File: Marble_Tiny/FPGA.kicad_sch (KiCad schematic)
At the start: 43 parts, among them T1 BSS138LT1G, T2 BSS138LT1G, U1 XC7A35T-CSG325, U28 24AA256UID-I_ST

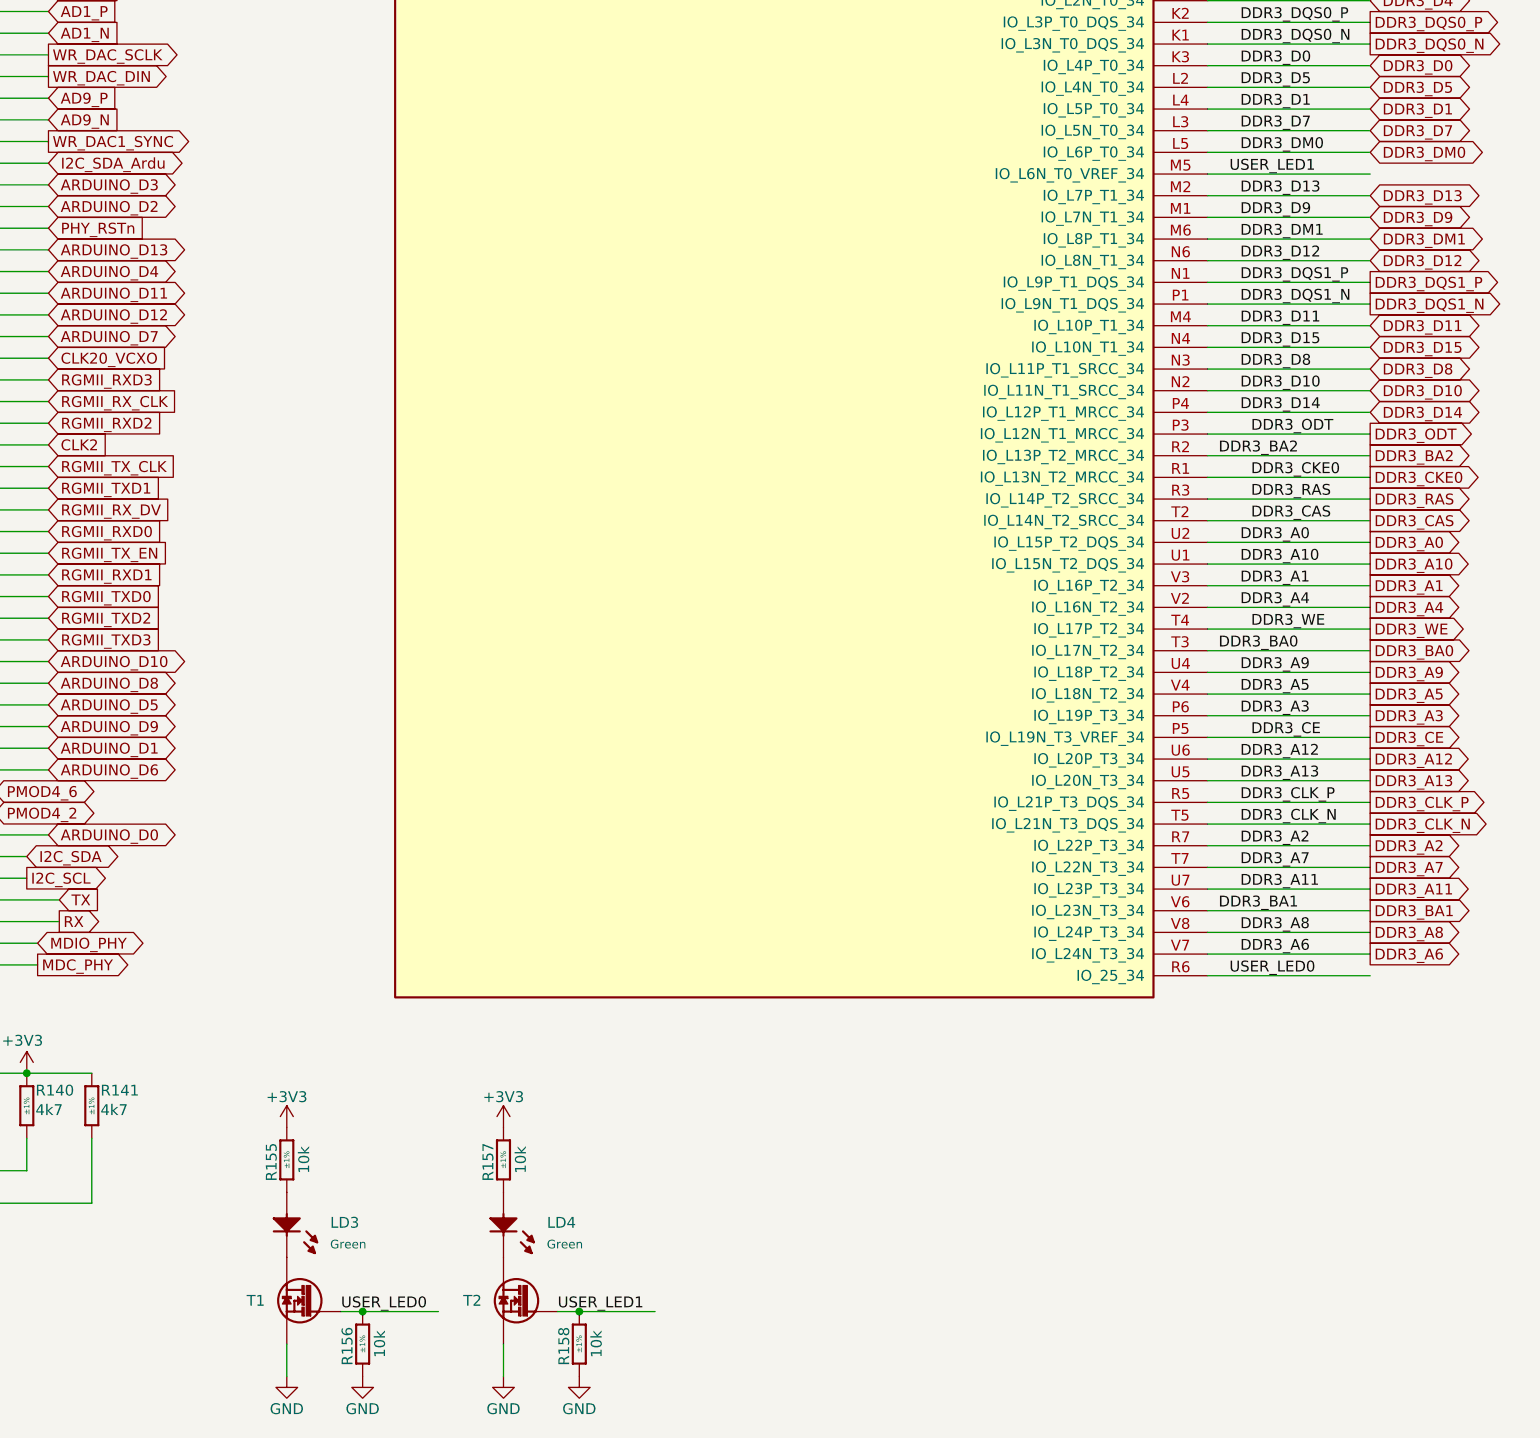
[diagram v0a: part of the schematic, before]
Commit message: connected more address lines to DDR, new board name
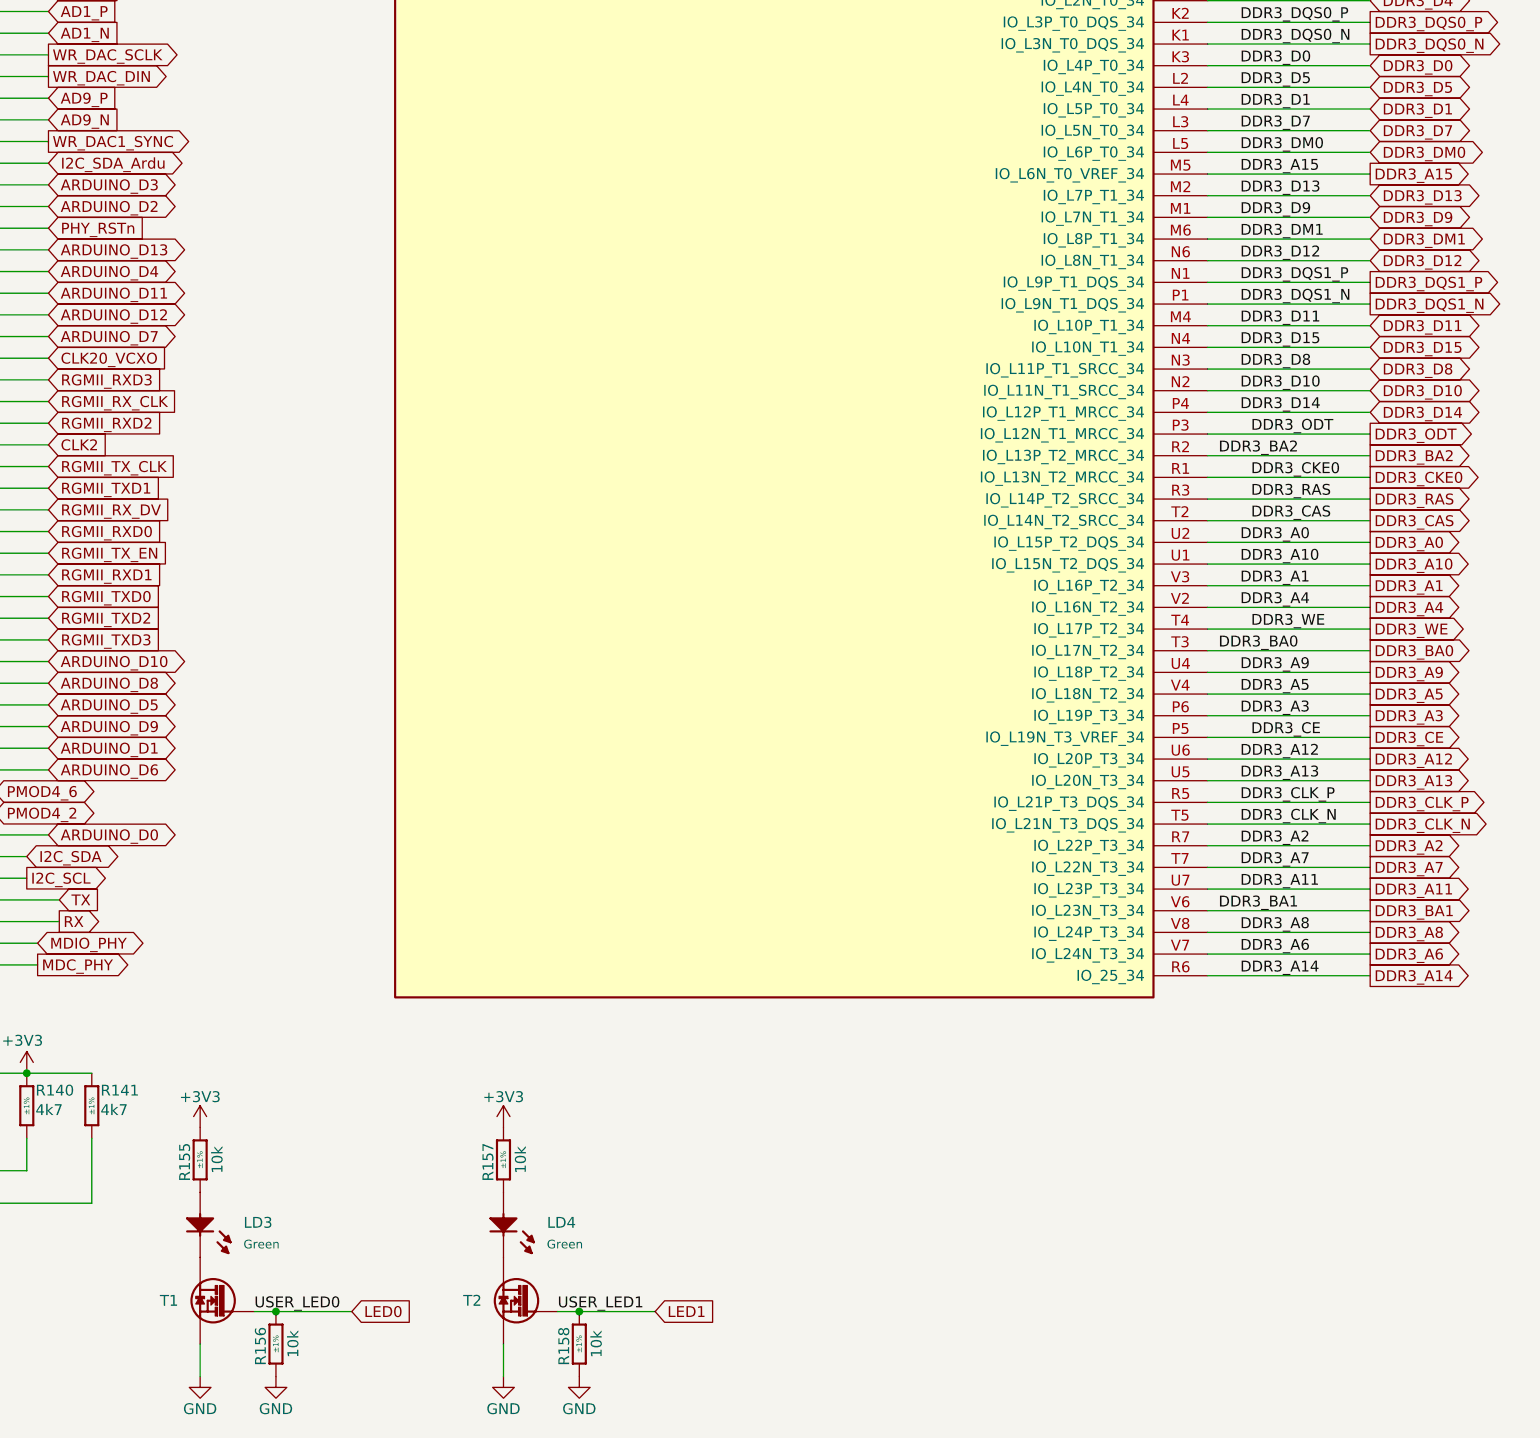
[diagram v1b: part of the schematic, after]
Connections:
- net USER_LED0 renamed LED0
- net LED0: no longer U1.R6 (IO_25_34)
- net USER_LED1 renamed LED1
- net LED1: no longer U1.M5 (IO_L6N_T0_VREF_34)
- new net DDR3_A14: U1.R6 (IO_25_34)
- new net DDR3_A15: U1.M5 (IO_L6N_T0_VREF_34)
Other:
- moved on the sheet: LD3, R155, R156, T1

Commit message: ready for the final review
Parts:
- added R182: R0402_4K7_1%_0.0625W_100PPM, Resistors SMD:RESC1005X40N, symbol Resistors SMD:R0402_4K7_1%_0.0625W_100PPM
- added SW2: SW_DIP_x01, Switches:SW_OMRON_A6SN-1101, symbol Switch:SW_DIP_x01
- renumbered T1 to Q1, T2 to Q2
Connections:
- net +3V3: now also R182.2
- net AD9_P: now also SW2.1
- net MDIO_PHY: now also R182.1
- new net RTS: SW2.2
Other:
- moved on the sheet: C227, R139, R140, R141, TP2, TP3, U28
